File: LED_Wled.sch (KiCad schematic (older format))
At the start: 46 parts, among them J1 SWD_PORT_SKEDD, J2 Barrel_Jack, J3 LED_pigtail JST-SM, J4 Conn_01x04, Q1 BSS138, Q2 AO4485, Q4 AO4485, Q5 AO4485, U1 ESP32-WROOM-32, U2 TPS5450DDAR, U3 LM1117-3.3

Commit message: pcb drawn, changed components
lm1117 to ams1117
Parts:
- C1: Description [Basic] X7R ±10% 50V 10nF 0603 Multilayer Ceramic Capacitor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 -> [Basic] 50V 10nF X7R ±10% 0603 Multilayer Ceramic Capacitor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; MPN (none) -> 0603B103K500NT
- C10, C12, C7: Description [Basic] X7R 100nF ±10% 50V 0603 Multilayer Ceramic Capacito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 -> [Basic] 50V 100nF X7R ±10% 0603 Multilayer Ceramic Capacito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; MPN (none) -> CC0603KRX7R9BB104
- C11, C4, C5, C8, C9: Description [Basic] X5R ±10% 50V 10uF 1206 Multilayer Ceramic Capacitor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 -> [Basic] 50V 10uF X5R ±10% 1206 Multilayer Ceramic Capacitor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; MPN (none) -> CL31A106KBHNNNE
- C2: Description SMD Aluminium Electrolytic Capacitor, Radial Can - SMD, 150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 -> [Extended] 16V 150uF ±20% 22mΩ@100kHz~300kHz 6.7mm 3.22A@10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; JLCPCB_CORRECTION (none) -> 0;0;180; MFR PANASONIC -> Lelon; MPN (none) -> OVZ151M1CTR-0807
- C3: Description None -> [Extended] 2000hrs@105℃ -45℃~+105℃ 22uF 5.4mm 16V 5mm ±20% 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; MFR None -> ROQANG; MPN (none) -> RVT1C220M0505
- C6: Description 22uF ±10% 10V 10 Ω @ 100kHz -55℃~125℃ CASE-A_3216 Tantalum 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 -> [Extended] 22uF 10V -55℃~+125℃ 10Ω@100kHz ±10% CASE-A_3216 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; JLCPCB_CORRECTION (none) -> 0;0;180; MPN (none) -> CA45-A-10V-22uF-K
- D1: Description Red 615~630nm 0805 Light Emitting Diodes (LED) RoHS -> [Basic] Red 0805 Light Emitting Diodes (LED) ROHS; MPN (none) -> NCD0805R1
- D2: Description Schottky Rectifier, 60 V, 2 A, Single, SOD-123FL, 2 Pins, 6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 -> [Basic] 0.5mA@40V 40V Single 3A 0.55V@3A SMA(DO-214AC) Scho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; JLCPCB_CORRECTION (none) -> 0;0;-180; MFR ONSEMI -> MDD（Microdiode Electronics）; MPN (none) -> SS34
- D3: Description SOD-123FL Diodes - General Purpose RoHS -> [Basic] 1A 10μA@1kV 1kV 1.1V@1A SOD-123FL Diodes - General 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; JLCPCB_CORRECTION (none) -> 0;0;-180; MFR MDD(Microdiode Electronics) -> MDD（Microdiode Electronics）; MPN (none) -> SM4007PL
- D4: Description [Extended] Bidirectional 9.5A 42.1V 28.9V 26V SMA(DO-214AC)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 -> [Extended] 9.5A 42.1V 28.9V 26V Bi-Directional SMA(DO-214AC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; JLCPCB_CORRECTION (none) -> 0;0;-180; MPN (none) -> SMAJ26CA
- D5: renamed from D?; Description (none) -> [Extended] 100nA@10.5V 30Ω Single 14.7V~15.3V 500mW 15V SOD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; JLCPCB_CORRECTION (none) -> 0;0;-180; JLCSMT BZT52C15 -> C179512; JLCSMT_PKG SOT-23-3 -> SOD-123; MFR (none) -> Suzhou Good-Ark Elec; MPN (none) -> BZT52B15
- D6: renamed from D?; Description Schottky Rectifier, 60 V, 2 A, Single, SOD-123FL, 2 Pins, 6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 -> [Basic] 0.5mA@40V 40V Single 3A 0.55V@3A SMA(DO-214AC) Scho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; JLCPCB_CORRECTION (none) -> 0;0;-180; MFR ONSEMI -> MDD（Microdiode Electronics）; MPN (none) -> SS34
- J2: Description (none) -> [Extended] 2mm 6.4mm 500mA 30V Plugin AC/DC Power Connector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; MFR (none) -> Korean Hroparts Elec; MPN (none) -> DC-005-20A
- J3: Description (none) -> [Extended] Shrouded Square Pins 2.54mm 6mm -40℃~+105℃ 1 3 2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; MFR (none) -> CJT(Changjiang Connectors); MPN (none) -> A2541WR-3P
- J4: Description (none) -> [Extended] 3A Shrouded Square Pins 2.54mm 6mm -55℃~+105℃ 1 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; MFR (none) -> BOOMELE(Boom Precision Elec); MPN (none) -> C91552
- L1: Description [Extended] 5A 22uH ±20% 58mΩ SMD Power Inductors ROHS -> [Extended] 5A 22uH ±20% 58mΩ SMD Power Inductors ROHS; MPN (none) -> FXL1040-220-M
- L2: Description Power Inductor (SMD), AEC-Q200, 3.3 µH, 6.6 A, Shielded, 5.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 -> [Extended] 6A 3.3uH ±20% 20mΩ SMD,7.1x6.6x3mm Power Inducto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; MFR COILCRAFT -> YJYCOIN; MPN (none) -> YSPI0630A-3R3M
- L3: symbol userdvc:ACM1211 -> LED_Wled-rescue:ACM1211-userdvc; Description Filter, Common Mode, ACM Series, 1 kohm, 6 A, 12mm x 11mm x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 -> [Extended] 2 -40℃~+85℃ 6A 14mΩ 80V 1kΩ @ 100MHz SMD,12x11mm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; MPN (none) -> ACM1211-102-2PL-TL01
- Q1: Description (none) -> [Extended] 50V 220mA 3.5Ω@10V,220mA 360mW 1.5V@1mA N Channe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; JLCPCB_CORRECTION (none) -> 0;0;180; MFR - -> Yangzhou Yangjie Elec Tech; MPN (none) -> BSS138
- Q2, Q4, Q5: Description (none) -> [Extended] 40V 10A 1.7W 15mΩ@10V,10A 2.5V@250μA P Channel S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; JLCPCB_CORRECTION (none) -> 0;0;-90; MFR (none) -> Alpha & Omega Semicon; MPN (none) -> AO4485
- Q3: renamed from Q?; Description (none) -> [Basic] 40V 200mW 200mA 100@10mA,1V 300MHz 300mV@50mA,5mA N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; JLCPCB_CORRECTION (none) -> 0;0;180; JLCSMT_PKG C20526 -> SOT-23-3; MFR (none) -> Jiangsu Changjing Electronics Technology Co., Ltd.; MPN (none) -> MMBT3904
- R1, R3, R4, R5: Description (none) -> [Basic] 1/8W Thick Film Resistors 150V ±1% ±100ppm/℃ -55℃~+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; MFR - -> UNI-ROYAL(Uniroyal Elec); MPN (none) -> 0805W8F1002T5E
- R10: renamed from R?; Description (none) -> [Basic] 1/8W Thick Film Resistors 150V ±1% ±100ppm/℃ -55℃~+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; MFR - -> UNI-ROYAL(Uniroyal Elec); MPN (none) -> 0805W8F1002T5E
- R2: Description [Basic] ±1% 4.7kΩ ±100ppm/℃ 0.1W 0603 Chip Resistor - Surfa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 -> [Basic] 1/10W Thick Film Resistors 75V ±1% ±100ppm/℃ -55℃~+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; MPN (none) -> 0603WAF4701T5E
- R6: renamed from R?; Description [Basic] ±1% 4.7kΩ ±100ppm/℃ 0.1W 0603 Chip Resistor - Surfa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 -> [Basic] 1/10W Thick Film Resistors 75V ±1% ±100ppm/℃ -55℃~+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; MPN (none) -> 0603WAF4701T5E
- R7: renamed from R?; Description (none) -> [Basic] 1/10W Thick Film Resistors 75V ±1% ±100ppm/℃ -55℃~+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; MFR - -> UNI-ROYAL(Uniroyal Elec); MPN (none) -> 0603WAF2401T5E
- R8: Description 1/10W Thick Film Resistors 75V ±1% ±100ppm/℃ -55℃~+155℃ 15k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 -> [Basic] 1/10W Thick Film Resistors 75V ±1% ±100ppm/℃ -55℃~+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; MFR NEOHM - TE CONNECTIVITY -> UNI-ROYAL(Uniroyal Elec); MPN (none) -> 0603WAF1502T5E
- R9: Description [Basic] ±1% 4.7kΩ ±100ppm/℃ 0.1W 0603 Chip Resistor - Surfa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 -> [Basic] 1/10W Thick Film Resistors 75V ±1% ±100ppm/℃ -55℃~+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; MFR MULTICOMP PRO -> UNI-ROYAL(Uniroyal Elec); MPN (none) -> 0603WAF4701T5E
- U1: Description (none) -> [Extended] SMD38,18x25.5x3.1 WiFi Modules ROHS; MFR (none) -> Espressif Systems; MPN (none) -> ESP32-WROOM-32E(8MB)
- U2: Description 36V 5A SOP-8_EP_150mil DC-DC Converters RoHS -> [Extended] Step-down type SOP-8EP_150mil DC-DC Converters R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; JLCPCB_CORRECTION (none) -> 0;0;-90; JLCSMT_PKG SOP-8_EP_150mil -> SOP-8_EP_3.9x4.9x1.27P; MPN (none) -> TPS5450DDAR
- U3: value LM1117-3.3 -> AMS1117-3.3; Description Fixed 15V 3.3V 1.2V @ 800mA SOT-223 Dropout Regulators(LDO)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 -> [Basic] 72dB@(120Hz) 1A 1.3V@(800mA) Fixed 3.3V~3.3V Positi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; JLCPCB_CORRECTION (none) -> 0;0;180; JLCSMT C9662 -> C6186; MFR Texas Instruments -> Advanced Monolithic Systems; MPN (none) -> AMS1117-3.3
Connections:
- net labels added: LED_OUT_HS1, LED_OUT_LS1, LED_VOUT_LS1, PWR_Line
- net labels removed: LED_OUT_HV, LED_OUT_LV, LED_VOUT_SWL, VIN
- wire segments 219 -> 216
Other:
- moved on the sheet: D5, D6, J1, J2, J3, J4, Q2, Q3, Q4, Q5, R10, R6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

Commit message: test
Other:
- note added: "test"
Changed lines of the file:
@@
 Text GLabel 2350 750  0    50   Input ~ 0
 Vin
-Text GLabel 3800 2650 2    50   Input ~ 0
-LED_VOUT
 Wire Wire Line
 	2800 950  2800 1200
@@
 	1300 1850 1450 1850
 Wire Wire Line
-	3750 2650 3800 2650
-Connection ~ 3750 2650
-Wire Wire Line
 	2400 1350 2400 1500
 Connection ~ 2400 1500
@@
 	0    1    1    0
 $EndComp
+Connection ~ 3750 2650
+Wire Wire Line
+	3750 2650 3800 2650
+Text GLabel 3800 2650 2    50   Input ~ 0
+LED_VOUT
+Text Notes 6050 2850 0    50   ~ 0
+test
 $EndSCHEMATC

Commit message: connector changes, pcb redesign
added +5V output with switch with mosfet, changed level shifter from transistor to buffer 4chan, added 2 more led strip channels
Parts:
- removed Q1: BSS138, Package_TO_SOT_SMD:SOT-23, symbol Transistor_FET:BSS138
- removed R4, R5: 10k, Resistor_SMD:R_0805_2012Metric, symbol Device:R_Small
- added D7: SS34, Diode_SMD:D_SMA, symbol Device:D_Schottky
- added J5: LED_signal_chan, Connector_PinHeader_2.54mm:PinHeader_1x03_P2.54mm_Horizontal, symbol Connector_Generic:Conn_01x03
- added J6: +5V Out, Connector_PinHeader_2.54mm:PinHeader_1x02_P2.54mm_Horizontal, symbol Connector_Generic:Conn_01x02
- added Q1: AO4485, Package_SO:SOIC-8_3.9x4.9mm_P1.27mm, symbol LED_Wled:AO4485
- added U4: SN74HC125DR, Package_SO:SOIC-14_3.9x8.7mm_P1.27mm, symbol LED_Wled:SN74HC125DR
- J3: value LED_pigtail JST-SM -> VIN-Out; footprint Connector_PinHeader_2.54mm:PinHeader_1x03_P2.54mm_Horizontal -> Connector_PinHeader_2.54mm:PinHeader_1x02_P2.54mm_Horizontal; symbol Connector_Generic:Conn_01x03 -> Connector_Generic:Conn_01x02; Description [Extended] Shrouded Square Pins 2.54mm 6mm -40℃~+105℃ 1 3 2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 -> [Extended] Shrouded Square Pins 2.5mm 6mm -40℃~+105℃ 1 2 2.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; JLCSMT C225489 -> C492410; JLCSMT_PKG HDR-TH_3P-P2.54-H-W10.0 -> HDR-TH_2P-P2.54-H-M-W10.4; MFR CJT(Changjiang Connectors) -> XFCN; MPN A2541WR-3P -> PZ254R-11-02P
- J4: value Conn_01x04 -> Microphone input
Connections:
- net +5V: now also Q1.1 (S), Q1.2 (S), Q1.3 (S), U4.1 (1OE), U4.10 (3OE), U4.14 (VCC), U4.4 (2OE)
- net GND: now also U4.7 (GND)
- net GNDPWR: now also J3.2 (Pin_2), J6.2 (Pin_2); no longer J3.3 (Pin_3)
- net LED_OUT_HS1: now also J5.1 (Pin_1), U4.3 (1Y); no longer J3.1 (Pin_1)
- net LED_OUT_LS1: now also U4.2 (1A)
- net LED_VOUT: now also J3.1 (Pin_1); no longer J3.2 (Pin_2)
- net LED_OUT_LS2: now reaches U1.14 (IO12)
- net LED_OUT_LS2: now also U4.5 (2A)
- net LED_OUT_LS3: now reaches U1.16 (IO13)
- net LED_OUT_LS3: now also U4.9 (3A)
- net at D5.2 (A), Q2.4 (G), Q3.3 (C)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: now also Q1.4 (G)
- net at D6.2 (A), Q3.2 (E), R10.2: now also D7.2 (A)
- net LED_VOUT_LS1 renamed LED_VOUT_SWS
- new net LED_5VOUT: D7.1 (K), J6.1 (Pin_1), Q1.5 (D), Q1.6 (D), Q1.7 (D), Q1.8 (D)
- new net LED_OUT_HS2: J5.2 (Pin_2), U4.6 (2Y)
- new net LED_OUT_HS3: J5.3 (Pin_3), U4.8 (3Y)
- no-connect marks 26 -> 27
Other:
- note removed: "test"
- moved on the sheet: J1, J2, J4

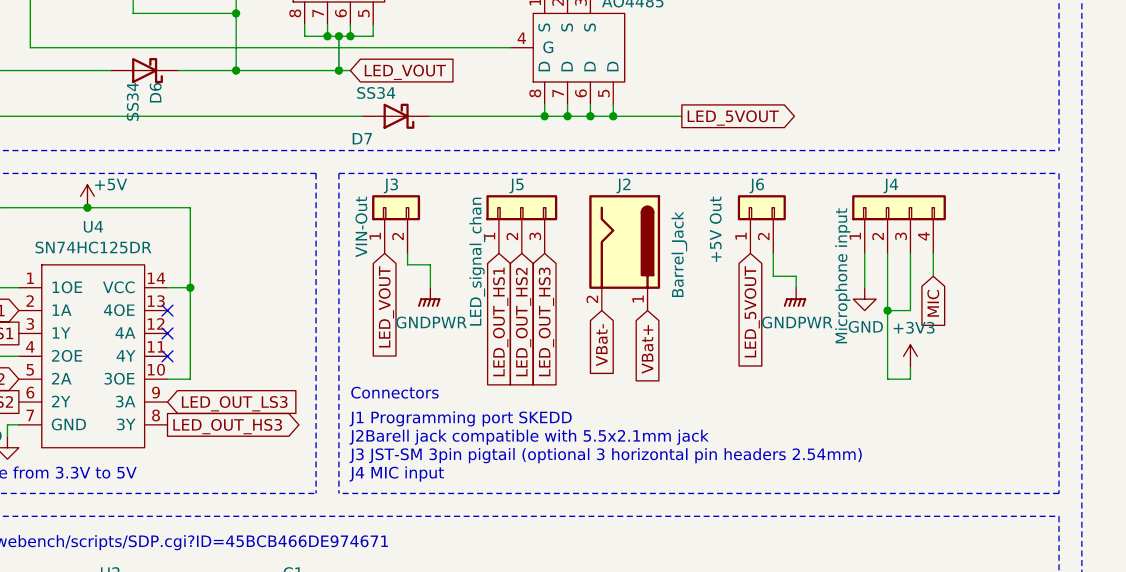
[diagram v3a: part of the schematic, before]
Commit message: redrawn pcb from scratch rev2.0
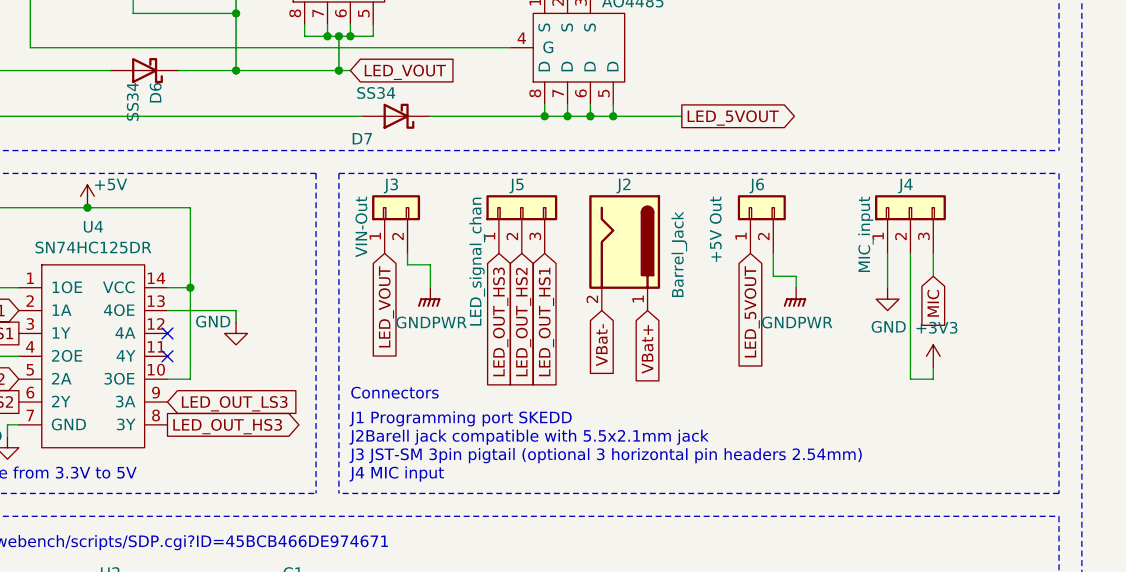
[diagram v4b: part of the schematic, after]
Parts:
- removed J4: Microphone input, Connector_PinHeader_2.54mm:PinHeader_1x04_P2.54mm_Horizontal, symbol Connector_Generic:Conn_01x04
- added J4: MIC_input, Connector_PinHeader_2.54mm:PinHeader_1x03_P2.54mm_Horizontal, symbol Connector_Generic:Conn_01x03
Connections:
- net +3V3: now also J4.2 (Pin_2)
- net GND: now also U4.13 (4OE), J4.1 (Pin_1)
- net LED_OUT_HS1: now also J5.3 (Pin_3); no longer J5.1 (Pin_1)
- net LED_OUT_HS3: now also J5.1 (Pin_1); no longer J5.3 (Pin_3)
- net MIC: now also J4.3 (Pin_3)
- no-connect marks 27 -> 26

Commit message: fixed +5v rail switch
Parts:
- removed D7: SS34, Diode_SMD:D_SMA, symbol Device:D_Schottky
- added D7: BZT52B15, Diode_SMD:D_SOD-123, symbol Diode:BZT52Bxx
- added D8: SS34, Diode_SMD:D_SMA, symbol Device:D_Schottky
- added Q6: MMBT3904, Package_TO_SOT_SMD:SOT-23, symbol Transistor_BJT:MMBT3904
- added R11: 10k, Resistor_SMD:R_0603_1608Metric, symbol Device:R_Small
- added R4: 4.7k, Resistor_SMD:R_0603_1608Metric, symbol Device:R
- added R5: 1k, Resistor_SMD:R_0603_1608Metric, symbol Device:R_Small
- L3: symbol LED_Wled-rescue:ACM1211-userdvc -> userdvc:ACM1211
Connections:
- net labels added: LED_VOUT_HSWS, LED_VOUT_LSWS
- net labels removed: LED_VOUT_SWS
- wire segments 242 -> 259
- no-connect marks 26 -> 24
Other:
- moved on the sheet: Q1
